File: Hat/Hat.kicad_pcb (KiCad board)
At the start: 4 copper layers, 85 x 56 mm, 58 parts, among them J1 Raspberry_Pi_2_3, J2 SWD, U1 ADUM3154, U2 ADUM3154, U3 ADUM3154, U4 ADUM3154, U5 STM32F411VETx, Y1 8MHz

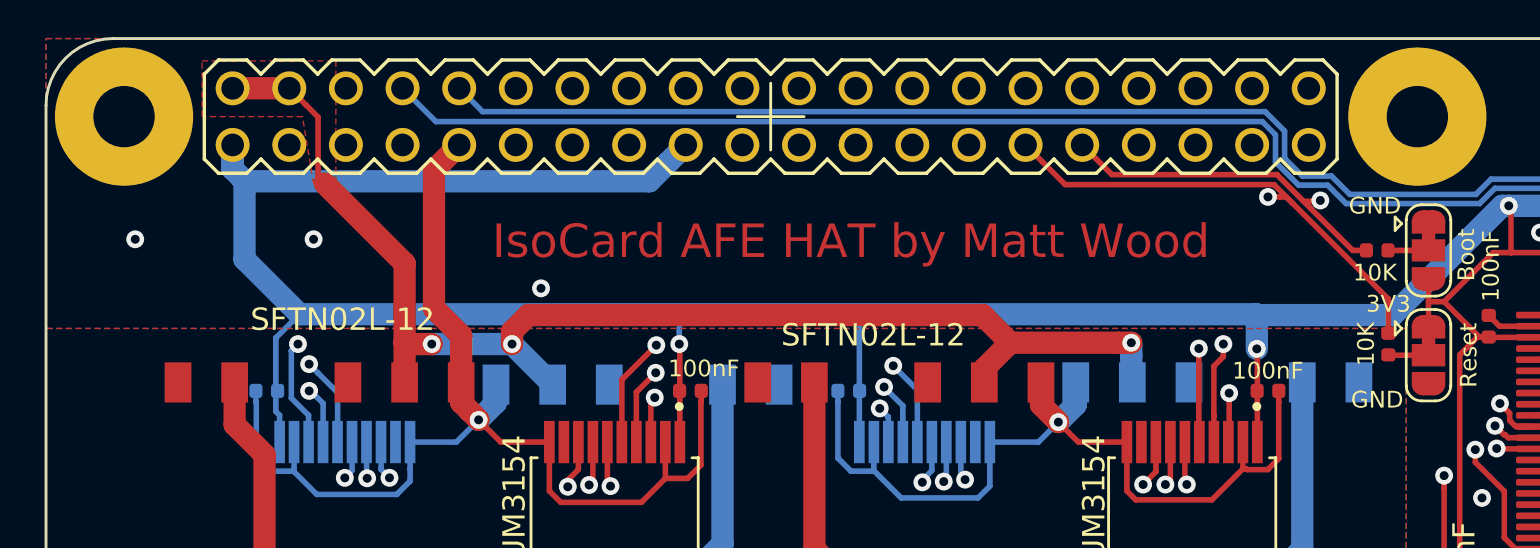
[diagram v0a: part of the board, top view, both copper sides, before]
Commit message: Added local regulator for rpi core reboot persistence
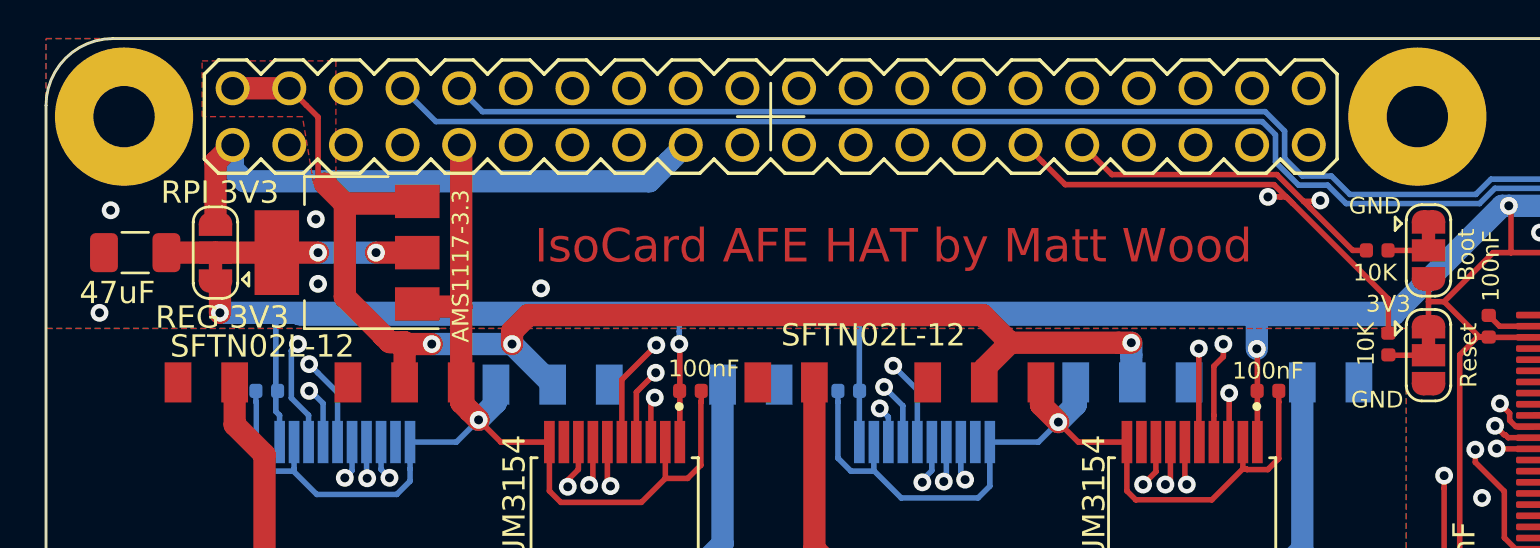
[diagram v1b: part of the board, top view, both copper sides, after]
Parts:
- added C23: 47uF, Capacitor_SMD:C_1206_3216Metric, F.Cu at (105.0, 76.6)
- added JP3: 3V3 SEL, Jumper:SolderJumper-3_P1.3mm_Bridged12_RoundedPad1.0x1.5mm, F.Cu at (108.6, 76.6)
- added U6: AMS1117-3.3, Package_TO_SOT_SMD:SOT-223-3_TabPin2, F.Cu at (114.5, 76.6)
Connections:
- J1 pad 1: +3V3 -> +3.3VP
- J1 pad 17: +3V3 -> +3.3VP
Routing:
- net +3V3: track 251.5 -> 325.2 mm, vias 7 -> 8
- net +3.3VP: track 0.00 -> 27.1 mm
- net Net-(C23-Pad1): track 0.00 -> 11.2 mm, vias 0 -> 2
- net +5V: track 58.6 -> 62.3 mm
- net GND: track 134.5 -> 136.7 mm, vias 25 -> 27
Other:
- board text added: "REG 3V3"
- board text added: "RPI 3V3"

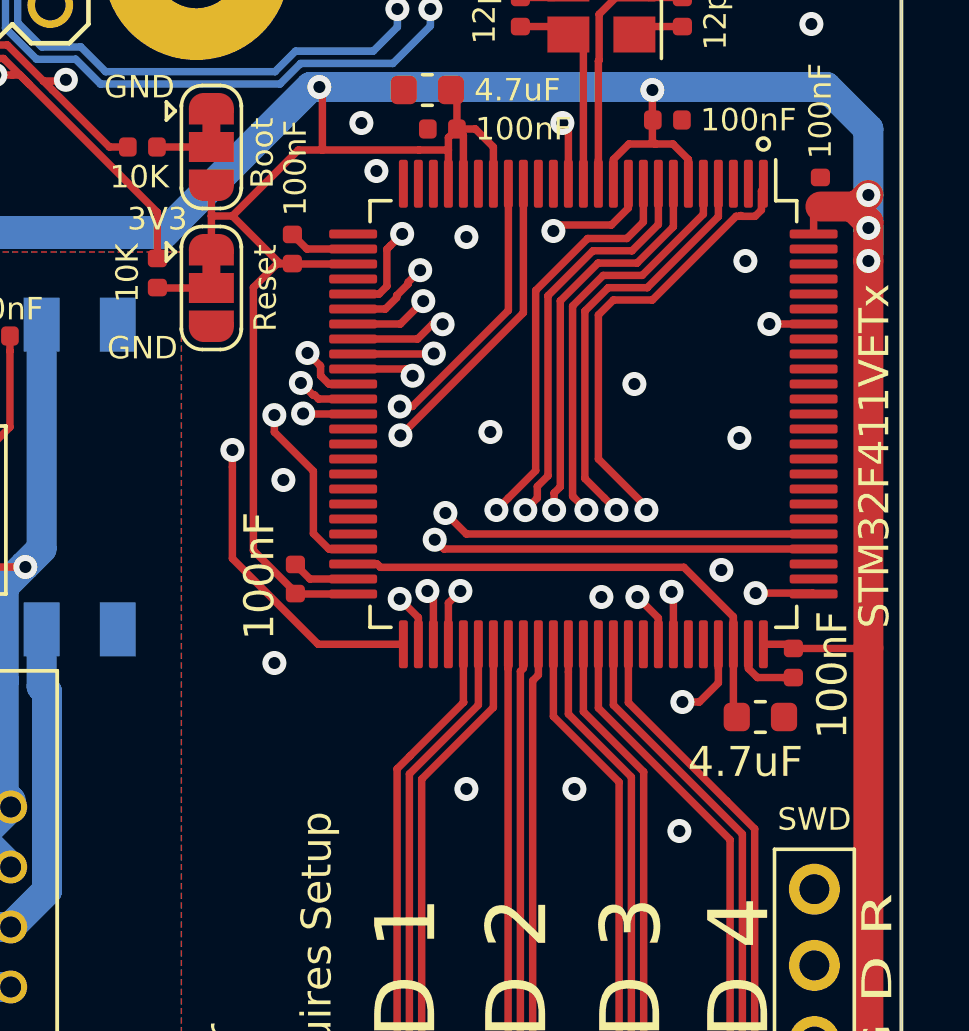
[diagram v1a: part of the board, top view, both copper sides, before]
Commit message: Added BOM to VC-01 and tidied silkscreen, added thermistor to hat. Regenerated gerbers & PDFs
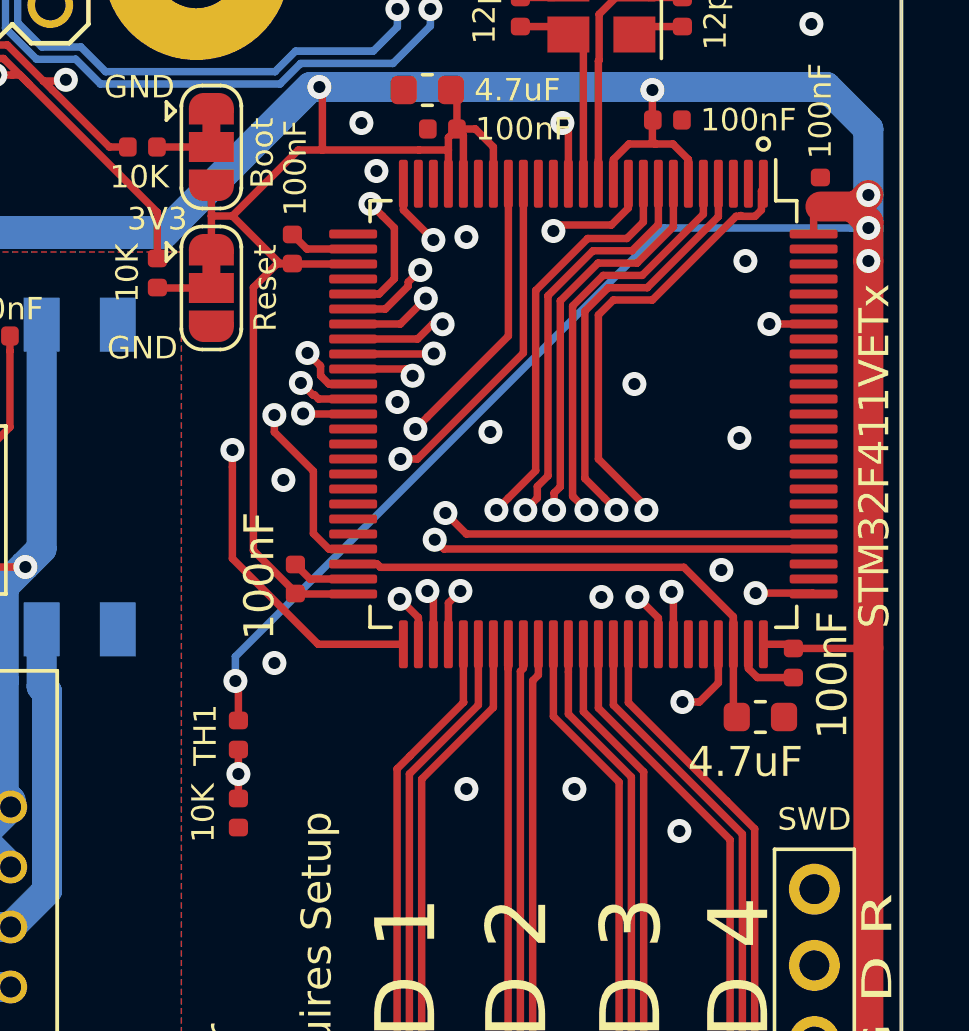
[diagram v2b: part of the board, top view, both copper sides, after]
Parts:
- added R15: 10K, Resistor_SMD:R_0402_1005Metric, F.Cu at (163.9, 98.7)
- added TH1: 10K, Resistor_SMD:R_0402_1005Metric, F.Cu at (163.9, 96.1)
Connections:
- U5 pad 25: (no net) -> /Board_Temp
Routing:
- net +3V3: track 325.2 -> 354.4 mm, vias 8 -> 9
- net /Board_Temp: track 0.00 -> 25.2 mm, vias 0 -> 2
- net /SPI2_MOSI: track 65.3 -> 63.0 mm
- net /SPI2_MISO: track 62.4 -> 60.6 mm
- net GND: vias 27 -> 28
